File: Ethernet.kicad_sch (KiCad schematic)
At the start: 8 parts, among them J2 RJ45_LINK-PP_LPJG0926HENL_Hor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, U12 TPD4EUSB30, U13 TPD4EUSB30

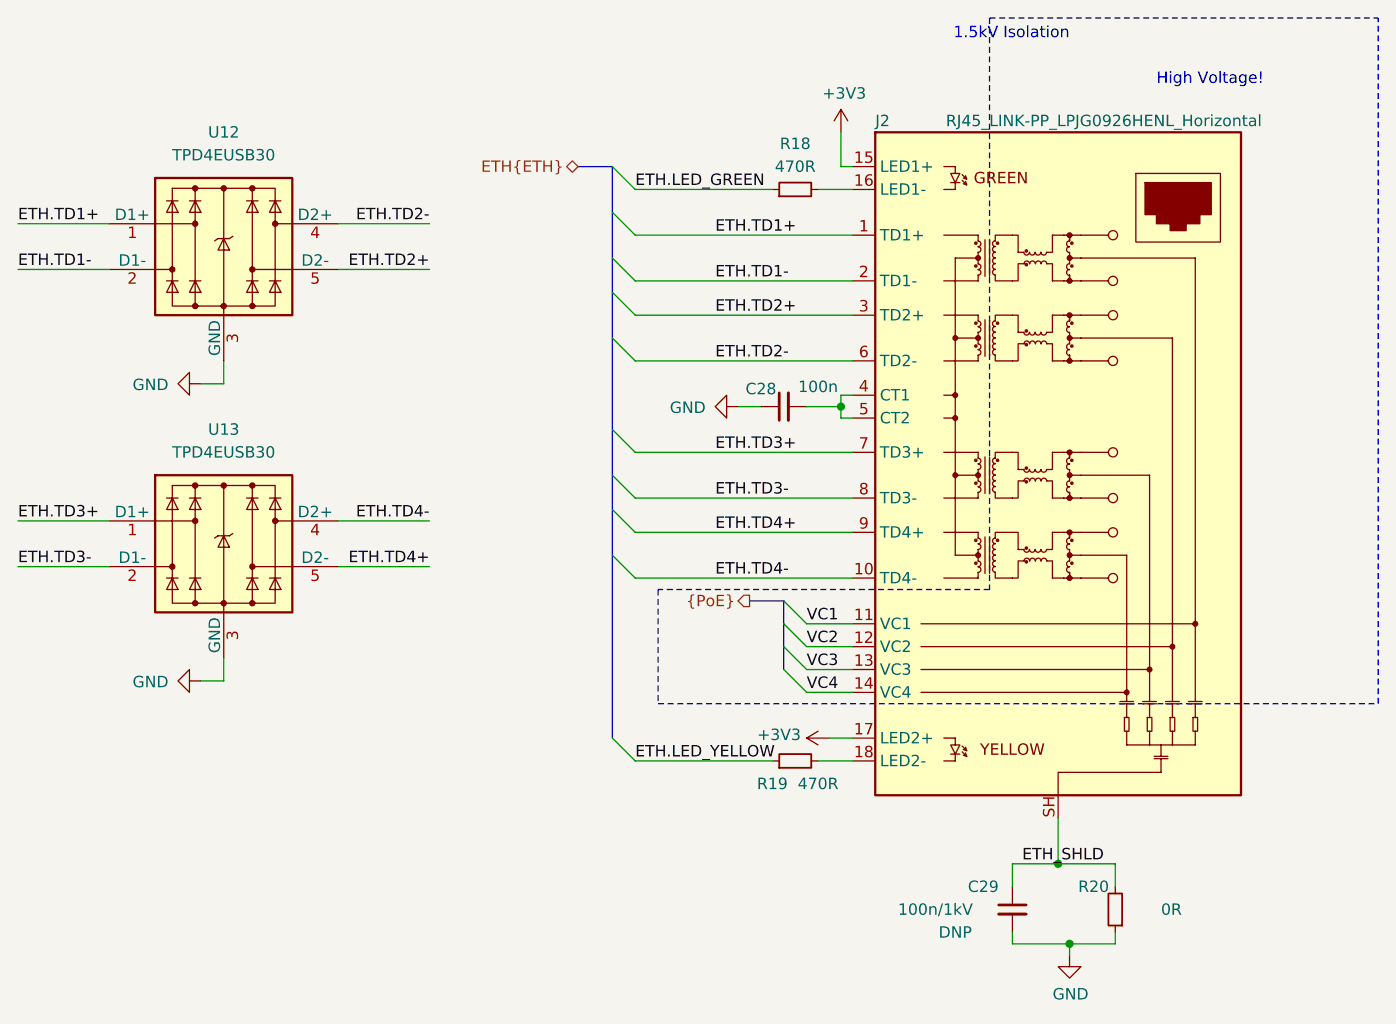
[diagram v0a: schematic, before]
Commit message: Reannotate the complete schematics
Signed-off-by: Stefan Agner <stefan@agner.ch>
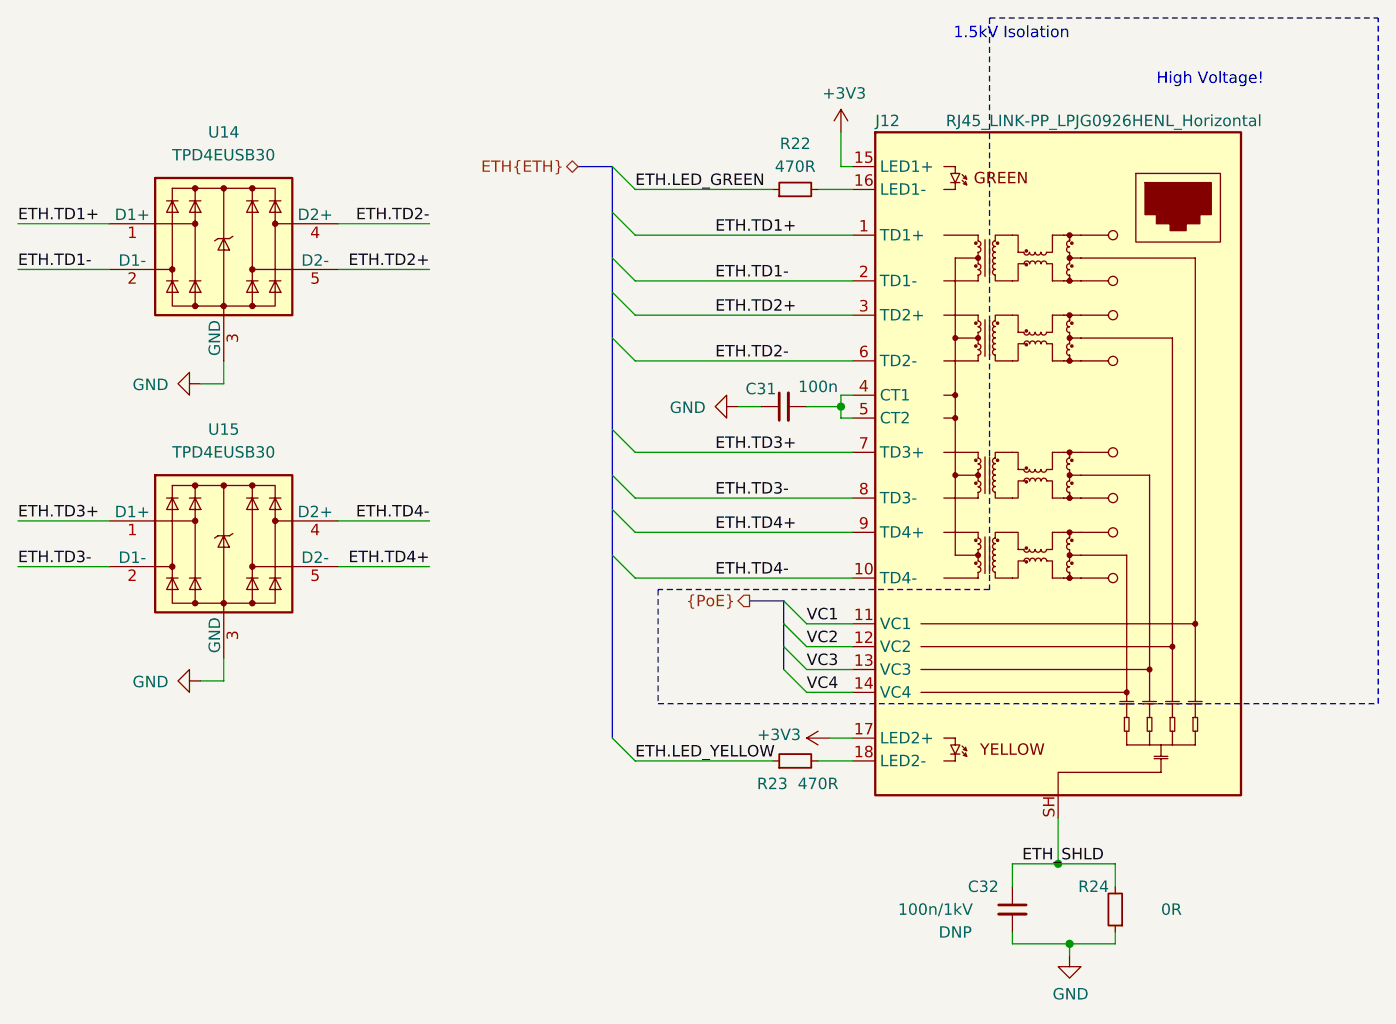
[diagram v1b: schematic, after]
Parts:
- renumbered C28 to C31, C29 to C32, J2 to J12, R18 to R22, R19 to R23, R20 to R24, U12 to U14, U13 to U15
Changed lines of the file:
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@@
   (symbol (lib_id "power:+3V3") (at 152.4 116.84 90) (unit 1)
     (in_bom yes) (on_board yes)
-    (property "Reference" "#PWR0182" (id 0) (at 156.21 116.84 0)
+    (property "Reference" "#PWR087" (id 0) (at 156.21 116.84 0)
       (effects (font (size 1.27 1.27)) hide)
     )
@@
   (symbol (lib_id "power:+3V3") (at 153.67 49.53 0) (unit 1)
     (in_bom yes) (on_board yes)
-    (property "Reference" "#PWR0184" (id 0) (at 153.67 53.34 0)
+    (property "Reference" "#PWR088" (id 0) (at 153.67 53.34 0)
       (effects (font (size 1.27 1.27)) hide)
     )
@@
   (symbol (lib_id "power:GND") (at 82.55 77.47 270) (unit 1)
     (in_bom yes) (on_board yes)
-    (property "Reference" "#PWR0181" (id 0) (at 76.2 77.47 0)
+    (property "Reference" "#PWR084" (id 0) (at 76.2 77.47 0)
       (effects (font (size 1.27 1.27)) hide)
     )
@@
   (symbol (lib_id "power:GND") (at 82.55 110.49 270) (unit 1)
     (in_bom yes) (on_board yes)
-    (property "Reference" "#PWR0180" (id 0) (at 76.2 110.49 0)
+    (property "Reference" "#PWR085" (id 0) (at 76.2 110.49 0)
       (effects (font (size 1.27 1.27)) hide)
     )
@@
   (symbol (lib_id "power:GND") (at 142.24 80.01 270) (unit 1)
     (in_bom yes) (on_board yes)
-    (property "Reference" "#PWR0183" (id 0) (at 135.89 80.01 0)
+    (property "Reference" "#PWR086" (id 0) (at 135.89 80.01 0)
       (effects (font (size 1.27 1.27)) hide)
     )
@@
   (symbol (lib_id "power:GND") (at 179.07 140.97 0) (unit 1)
     (in_bom yes) (on_board yes)
-    (property "Reference" "#PWR0179" (id 0) (at 179.07 147.32 0)
+    (property "Reference" "#PWR089" (id 0) (at 179.07 147.32 0)
       (effects (font (size 1.27 1.27)) hide)
     )
@@
   (symbol (lib_id "Device:R_Small") (at 148.59 55.88 90) (unit 1)
     (in_bom yes) (on_board yes)
-    (property "Reference" "R18" (id 0) (at 148.59 50.8 90))
+    (property "Reference" "R22" (id 0) (at 148.59 50.8 90))
     (property "Value" "470R" (id 1) (at 148.59 53.34 90))
     (property "Footprint" "Resistor_SMD:R_0402_1005Metric" (id 2) (at 148.59 55.88 0)
@@
   (symbol (lib_id "Device:R_Small") (at 148.59 119.38 90) (unit 1)
     (in_bom yes) (on_board yes)
-    (property "Reference" "R19" (id 0) (at 146.05 121.92 90))
+    (property "Reference" "R23" (id 0) (at 146.05 121.92 90))
     (property "Value" "470R" (id 1) (at 151.13 121.92 90))
     (property "Footprint" "Resistor_SMD:R_0402_1005Metric" (id 2) (at 148.59 119.38 0)
@@
   (symbol (lib_id "Device:R_Small") (at 184.15 135.89 180) (unit 1)
     (in_bom yes) (on_board yes)
-    (property "Reference" "R20" (id 0) (at 181.7432 133.35 0))
+    (property "Reference" "R24" (id 0) (at 181.7432 133.35 0))
     (property "Value" "0R" (id 1) (at 190.392 135.89 0))
     (property "Footprint" "Resistor_SMD:R_1206_3216Metric" (id 2) (at 184.15 135.89 0)
@@
   (symbol (lib_id "Device:C_Small") (at 147.32 80.01 90) (unit 1)
     (in_bom yes) (on_board yes)
-    (property "Reference" "C28" (id 0) (at 144.78 78.0477 90))
+    (property "Reference" "C31" (id 0) (at 144.78 78.0477 90))
     (property "Value" "100n" (id 1) (at 151.13 77.806 90))
     (property "Footprint" "Capacitor_SMD:C_0402_1005Metric" (id 2) (at 147.32 80.01 0)
@@
   (symbol (lib_id "Device:C_Small") (at 172.72 135.89 0) (unit 1)
     (in_bom yes) (on_board yes)
-    (property "Reference" "C29" (id 0) (at 169.4877 133.35 0))
+    (property "Reference" "C32" (id 0) (at 169.4877 133.35 0))
     (property "Value" "100n/1kV" (id 1) (at 164.166 135.89 0))
     (property "Footprint" "Capacitor_SMD:C_1206_3216Metric" (id 2) (at 172.72 135.89 0)
@@
   (symbol (lib_name "Power_Protection:TPD4EUSB30_1") (lib_id "LightBlue:TPD4EUSB30") (at 85.09 62.23 0) (unit 1)
     (in_bom yes) (on_board yes)
-    (property "Reference" "U12" (id 0) (at 85.09 49.53 0))
+    (property "Reference" "U14" (id 0) (at 85.09 49.53 0))
     (property "Value" "TPD4EUSB30" (id 1) (at 85.09 52.07 0))
     (property "Footprint" "Package_SON:USON-10_2.5x1.0mm_P0.5mm" (id 2) (at 60.96 72.39 0)
@@
   (symbol (lib_id "LightBlue:TPD4EUSB30") (at 85.09 95.25 0) (unit 1)
     (in_bom yes) (on_board yes)
-    (property "Reference" "U13" (id 0) (at 85.09 82.55 0))
+    (property "Reference" "U15" (id 0) (at 85.09 82.55 0))
     (property "Value" "TPD4EUSB30" (id 1) (at 85.09 85.09 0))
     (property "Footprint" "Package_SON:USON-10_2.5x1.0mm_P0.5mm" (id 2) (at 60.96 105.41 0)
@@
   (symbol (lib_id "LightBlue:RJ45_LINK-PP_LPJG0926HENL_Horizontal") (at 177.8 86.36 0) (unit 1)
     (in_bom yes) (on_board yes)
-    (property "Reference" "J2" (id 0) (at 157.48 48.26 0)
+    (property "Reference" "J12" (id 0) (at 157.48 48.26 0)
       (effects (font (size 1.27 1.27)) (justify left))
     )

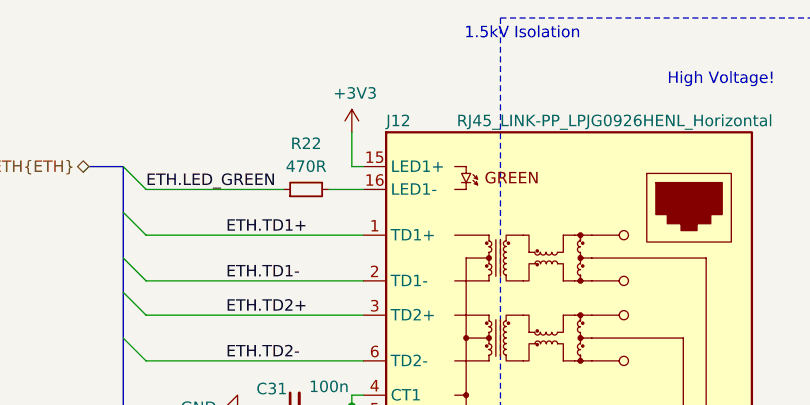
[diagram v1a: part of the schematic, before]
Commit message: Adjust rating/footprint size of some ceramic capacitors
Also update connector/jumper designator to make more sense.

Signed-off-by: Stefan Agner <stefan@agner.ch>
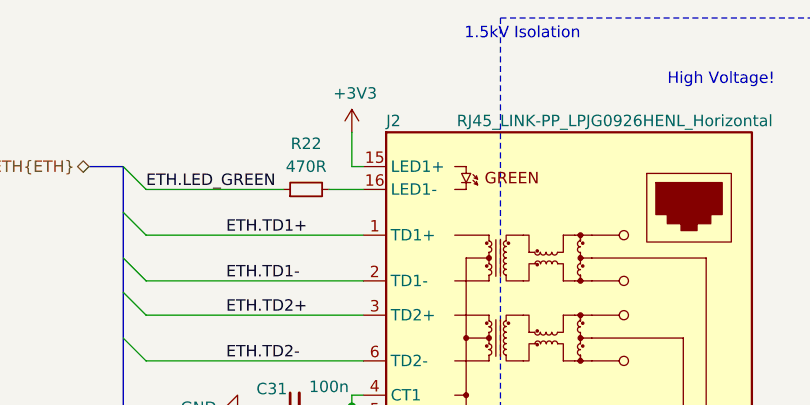
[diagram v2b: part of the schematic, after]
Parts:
- renumbered J12 to J2
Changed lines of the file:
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@@
   (symbol (lib_id "LightBlue:RJ45_LINK-PP_LPJG0926HENL_Horizontal") (at 177.8 86.36 0) (unit 1)
     (in_bom yes) (on_board yes)
-    (property "Reference" "J12" (id 0) (at 157.48 48.26 0)
+    (property "Reference" "J2" (id 0) (at 157.48 48.26 0)
       (effects (font (size 1.27 1.27)) (justify left))
     )

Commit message: Renmae LightBlue to Amber
Signed-off-by: Stefan Agner <stefan@agner.ch>
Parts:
- J2: footprint LightBlue:RJ45_LINK-PP_LPJG0926HENL_Horizontal -> Amber:RJ45_LINK-PP_LPJG0926HENL_Horizontal; symbol LightBlue:RJ45_LINK-PP_LPJG0926HENL_Horizontal -> Amber:RJ45_LINK-PP_LPJG0926HENL_Horizontal
- U14, U15: symbol LightBlue:TPD4EUSB30 -> Amber:TPD4EUSB30
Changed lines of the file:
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@@
     (company "Nabu Casa")
     (comment 1 "www.nabucasa.com")
-    (comment 2 "Light Blue")
+    (comment 2 "Amber")
   )
   (bus_alias "PoE" (members "VC1" "VC2" "VC3" "VC4"))
@@
     (pin "2")
   )
-  (symbol (lib_name "Power_Protection:TPD4EUSB30_1") (lib_id "LightBlue:TPD4EUSB30") (at 85.09 62.23 0) (unit 1)
+  (symbol (lib_name "Power_Protection:TPD4EUSB30_1") (lib_id "Amber:TPD4EUSB30") (at 85.09 62.23 0) (unit 1)
     (in_bom yes) (on_board yes)
     (property "Reference" "U14" (id 0) (at 85.09 49.53 0))
@@
     (pin "9")
   )
-  (symbol (lib_id "LightBlue:TPD4EUSB30") (at 85.09 95.25 0) (unit 1)
+  (symbol (lib_id "Amber:TPD4EUSB30") (at 85.09 95.25 0) (unit 1)
     (in_bom yes) (on_board yes)
     (property "Reference" "U15" (id 0) (at 85.09 82.55 0))
@@
     (pin "9")
   )
-  (symbol (lib_id "LightBlue:RJ45_LINK-PP_LPJG0926HENL_Horizontal") (at 177.8 86.36 0) (unit 1)
+  (symbol (lib_id "Amber:RJ45_LINK-PP_LPJG0926HENL_Horizontal") (at 177.8 86.36 0) (unit 1)
     (in_bom yes) (on_board yes)
     (property "Reference" "J2" (id 0) (at 157.48 48.26 0)
@@
     )
     (property "Value" "RJ45_LINK-PP_LPJG0926HENL_Horizontal" (id 1) (at 182.88 48.26 0))
-    (property "Footprint" "LightBlue:RJ45_LINK-PP_LPJG0926HENL_Horizontal" (id 2) (at 177.8 132.08 0)
-      (effects (font (size 1.27 1.27)) hide)
-    )
+    (property "Footprint" "Amber:RJ45_LINK-PP_LPJG0926HENL_Horizontal" (id 2) (at 177.8 132.08 0)
+      (effects (font (size 1.27 1.27)) hide)
+    )
